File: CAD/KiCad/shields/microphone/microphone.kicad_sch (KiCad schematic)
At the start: 0 parts

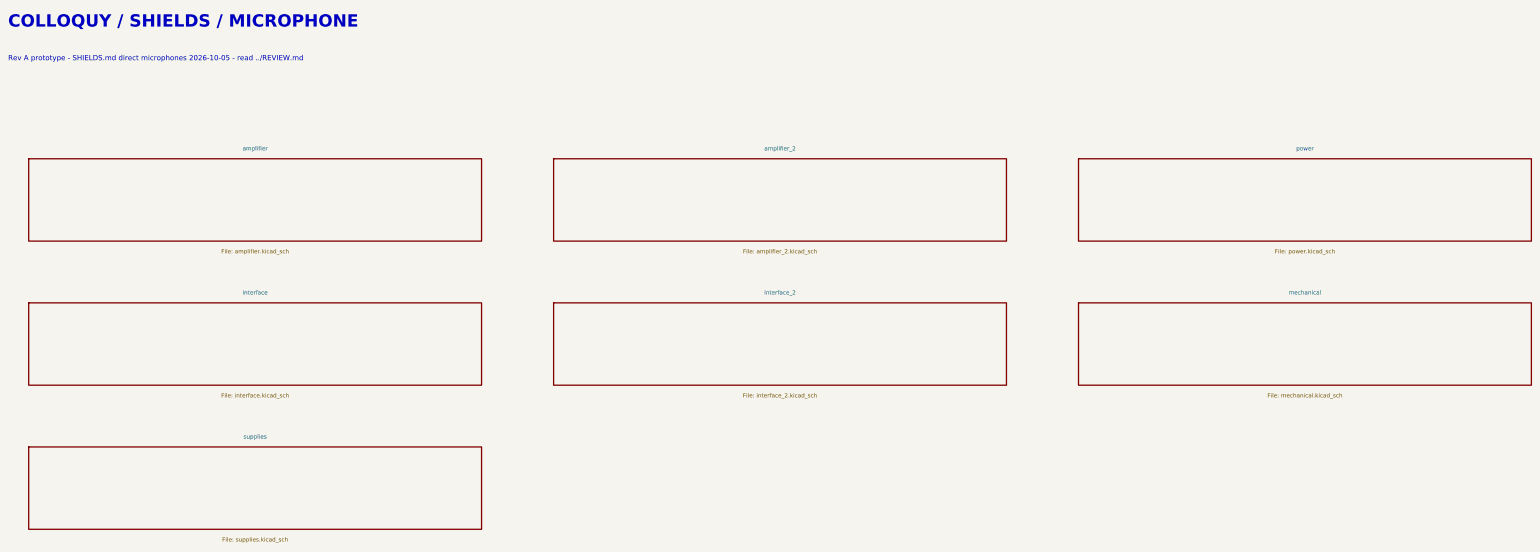
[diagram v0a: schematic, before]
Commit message: Mount the MAX9814 module on a socketed artwork holder
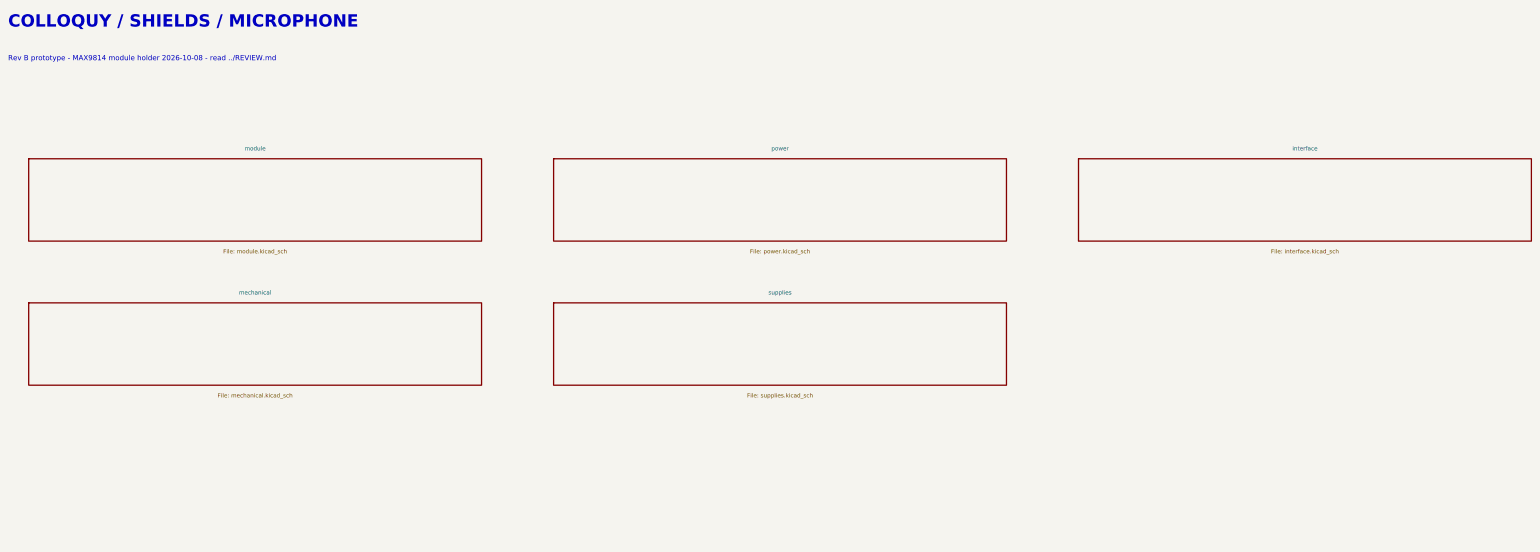
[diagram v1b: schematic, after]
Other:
- removed sheet amplifier
- removed sheet amplifier_2
- removed sheet interface_2
- added sheet module (module.kicad_sch)
- note added: "Rev B prototype - MAX9814 module holder 2026-10-08 - read ../REVIEW.md"
- note removed: "Rev A prototype - SHIELDS.md direct microphones 2026-10-05 - read ../REVIEW.md"
